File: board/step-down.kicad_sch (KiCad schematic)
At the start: 16 parts, among them U1 BD9G341AEFJ-E2

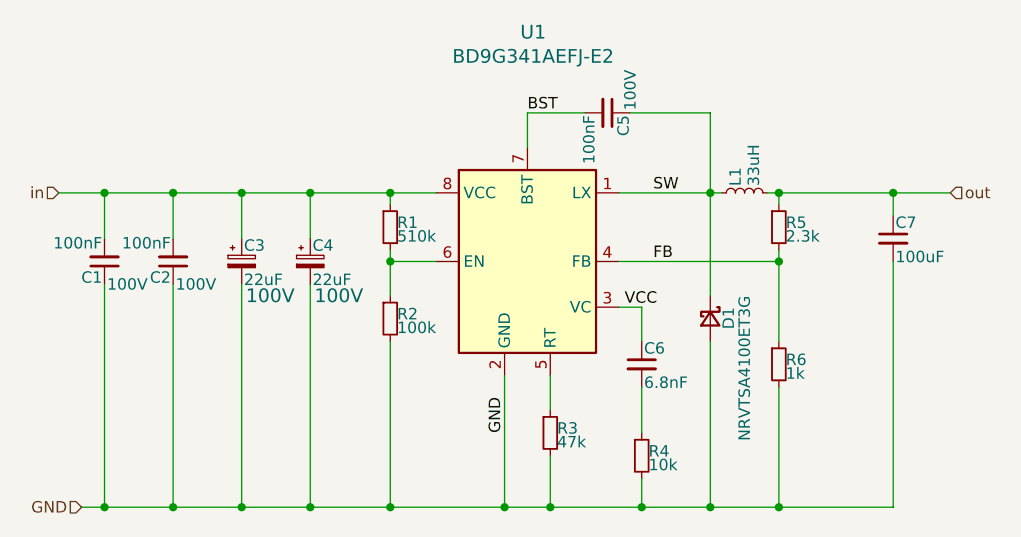
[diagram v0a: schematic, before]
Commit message: added lcsc part numbers
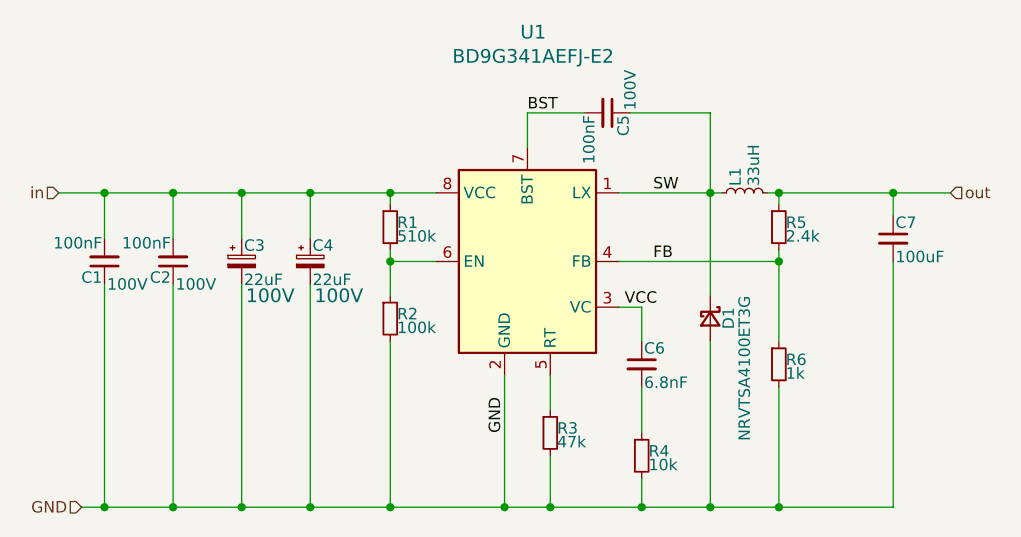
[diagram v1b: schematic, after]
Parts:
- C1, C2, C5: lcsc (none) -> C15725
- C3, C4: lcsc (none) -> C29144
- C6: lcsc (none) -> C1631
- C7: lcsc (none) -> C15008
- D1: lcsc (none) -> C413998
- L1: lcsc (none) -> C2983067
- R1: lcsc (none) -> C23192
- R2: lcsc (none) -> C25803
- R3: lcsc (none) -> C25819
- R4: lcsc (none) -> C25804
- R5: value 2.3k -> 2.4k; lcsc (none) -> C22940
- R6: lcsc (none) -> C21190
- U1: lcsc (none) -> C2981600
